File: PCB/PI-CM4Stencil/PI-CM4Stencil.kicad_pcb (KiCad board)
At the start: 2 copper layers, 40.2 x 55.2 mm, 1 part

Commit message: Created gerber files
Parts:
- removed REF**: Raspberry-Pi-4-Compute-Module, PI-CM4Stencil:Pi_CM4
- added U1: Pi_CM4, PI-CM4Stencil:Pi_CM4, F.Cu at (148.6, 97.8)

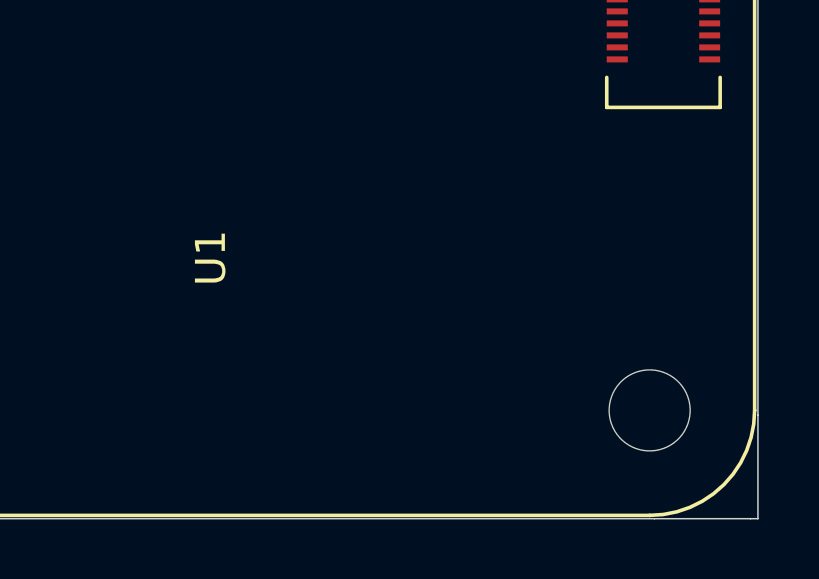
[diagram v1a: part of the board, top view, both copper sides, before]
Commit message: Revert "Created gerber files"
This reverts commit b53c7857d78f5a39796a9ae11ef4b5de09c35e59.
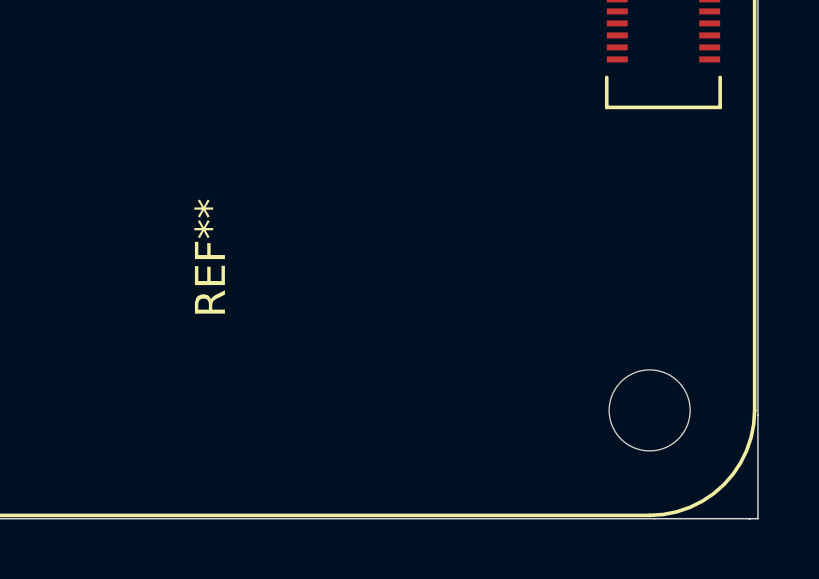
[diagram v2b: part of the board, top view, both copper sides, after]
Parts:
- removed U1: Pi_CM4, PI-CM4Stencil:Pi_CM4
- added REF**: Raspberry-Pi-4-Compute-Module, PI-CM4Stencil:Pi_CM4, F.Cu at (148.6, 97.8)
